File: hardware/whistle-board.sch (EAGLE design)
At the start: 17 parts, among them IC1 MCP4131, IC2 L272, Q1 BC638, Q3 BC638

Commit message: revisions after the most recent draft was assembled and tested
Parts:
- removed Q3: BC638, custom-parts:TRANSISTOR_PNPTO92
- removed R5: 1k, SparkFun-Resistors:1KOHM-1/4W-5%(PTH)
- removed SERIAL: (no value), SparkFun-Connectors:M03PTH
- AUX: device SparkFun-Connectors:M03PTH -> SparkFun-Connectors:M02PTH
- CTL: device SparkFun-Connectors:M02PTH -> SparkFun-Connectors:M04PTH
- Q1: value BC638 -> (none); device custom-parts:TRANSISTOR_PNPTO92 -> custom-parts:TRANSISTOR_NPNTO92
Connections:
- removed net 12V-EN: AUX.3, IC2.V+, Q1.C
- removed net EN: CTL.2, R4.1
- removed net N$5: Q3.B, R5.1
- net 12V: now also IC2.V+; no longer Q1.E
- net 5V: now also D1.C, S1.+; no longer Q3.E
- net CS: now also CTL.2; no longer SERIAL.1
- net DIR: now also R4.2; no longer R5.2
- net GND: now also Q1.E; no longer S1.-
- net N$1: now also Q1.C, S1.-; no longer Q1.B, R4.2
- net N$2: now also Q1.B, R4.1; no longer D1.C, Q3.C, S1.+
- net SCK: now also CTL.3; no longer SERIAL.2
- net SDI: now also CTL.4; no longer SERIAL.3
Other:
- moved on the sheet: D1, D2, IC1, IC2, POW, Q1, R1, R2, R3, R4, S1, TRACK

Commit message: sloppily terminating unused opamp
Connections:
- net GND: now also IC2.IN2+, IC2.IN2-
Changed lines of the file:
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@@
 <label x="58.42" y="66.04" size="1.778" layer="95"/>
+</segment>
+<segment>
+<pinref part="IC2" gate="G$1" pin="IN2+"/>
+<wire x1="25.4" y1="38.1" x2="27.94" y2="38.1" width="0.1524" layer="91"/>
+<label x="30.48" y="38.1" size="1.778" layer="95"/>
+</segment>
+<segment>
+<pinref part="IC2" gate="G$1" pin="IN2-"/>
+<wire x1="25.4" y1="35.56" x2="27.94" y2="35.56" width="0.1524" layer="91"/>
+<label x="30.48" y="35.56" size="1.778" layer="95"/>
 </segment>
 </net>
@@
 </sheet>
 </sheets>
-<errors>
-</errors>
 </schematic>
 </drawing>

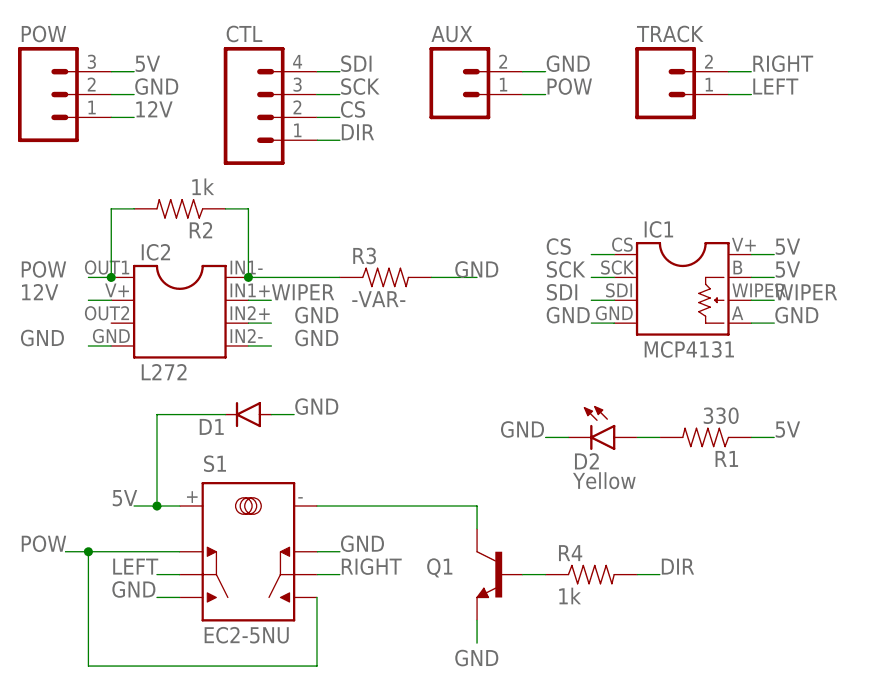
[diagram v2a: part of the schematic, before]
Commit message: adding/fixing diodes, adding silkscreen details
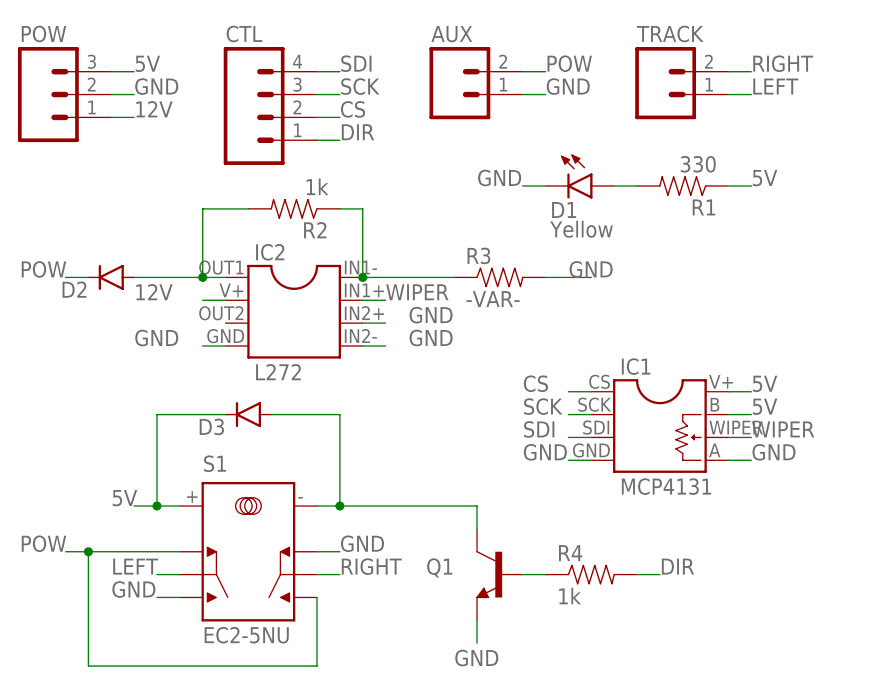
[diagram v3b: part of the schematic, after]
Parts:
- added D3: (no value), SparkFun-DiscreteSemi:DIODE1N4148
- D1: value (none) -> Yellow; device SparkFun-DiscreteSemi:DIODE1N4148 -> custom-parts:LED-YELLOW0603
- D2: value Yellow -> (none); device custom-parts:LED-YELLOW0603 -> SparkFun-DiscreteSemi:DIODEPTH
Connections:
- new net N$5: D2.A, IC2.OUT1, R2.2
- net 5V: now also D3.C; no longer D1.C
- net GND: now also AUX.1, D1.C; no longer AUX.2, D1.A, D2.C
- net N$1: now also D3.A
- net N$19: now also D1.A; no longer D2.A
- net POW: now also AUX.2, D2.C; no longer AUX.1, IC2.OUT1, R2.2
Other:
- moved on the sheet: IC1, IC2, R1, R2, R3

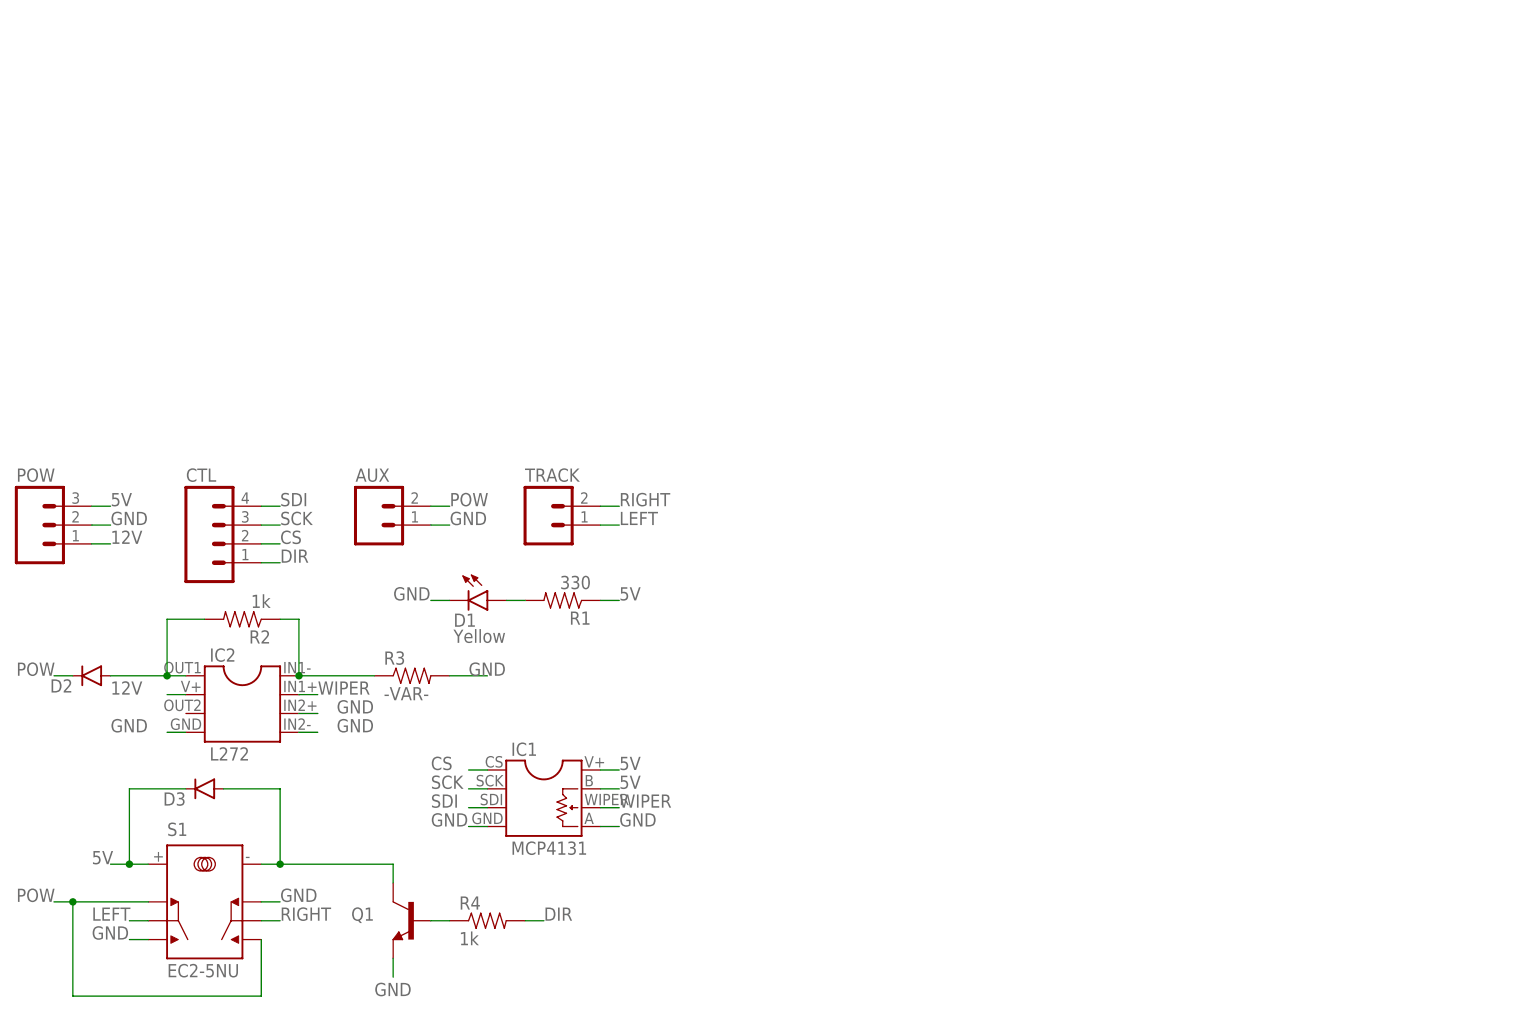
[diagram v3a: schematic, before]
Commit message: Updating license, annotating schematic, updating images, moving software
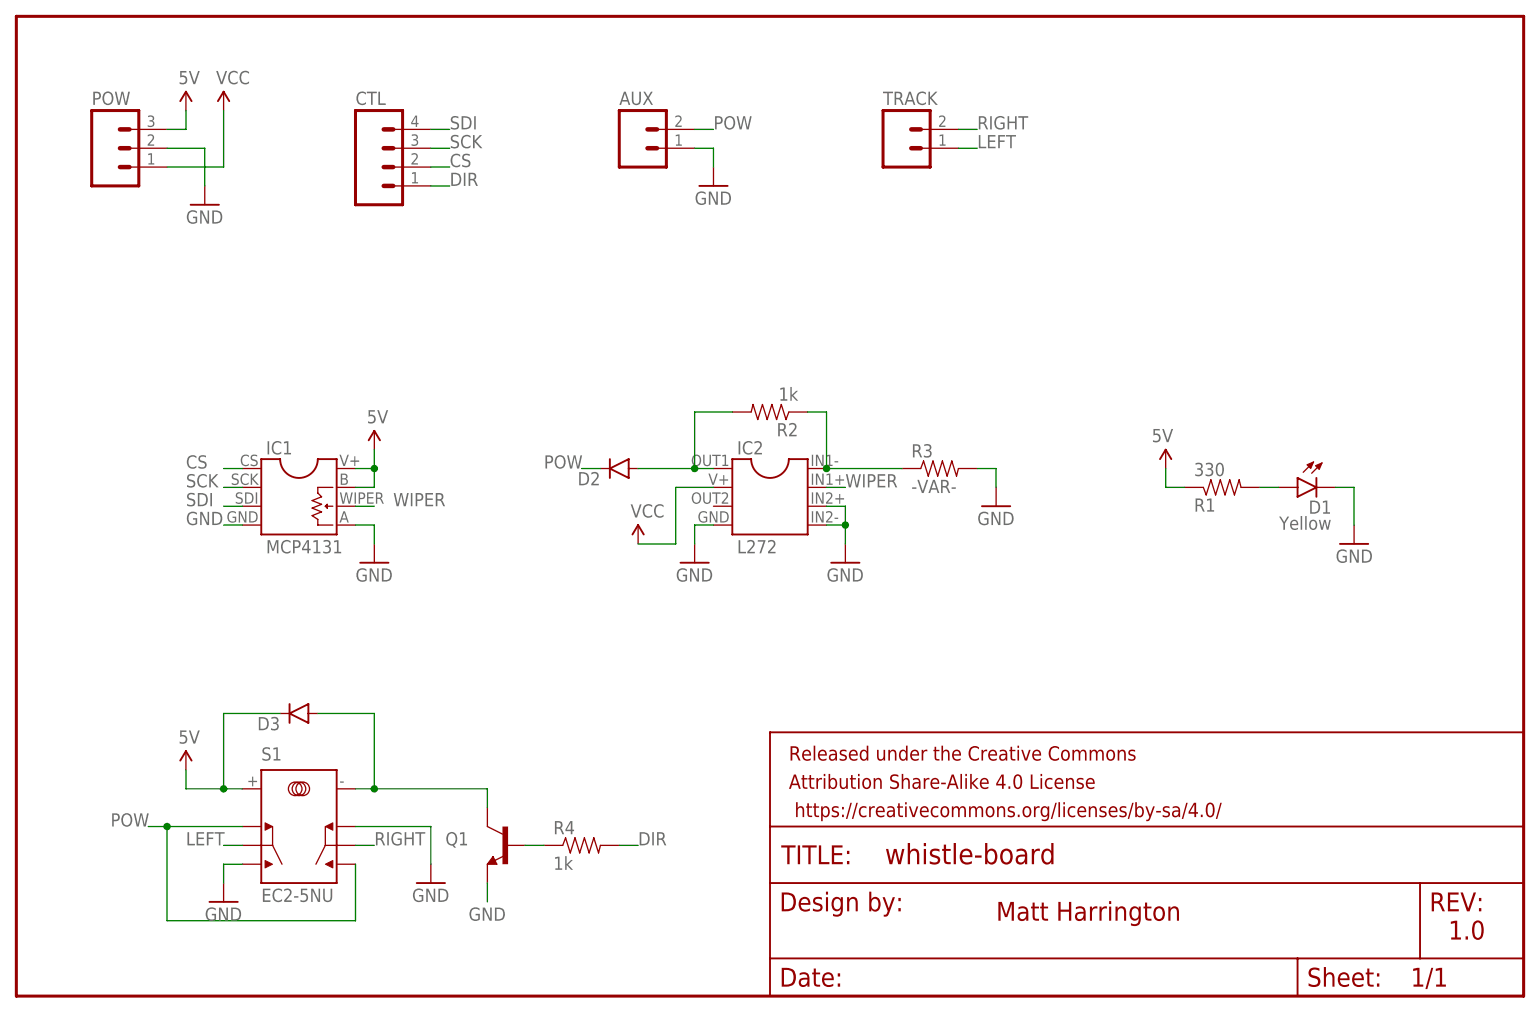
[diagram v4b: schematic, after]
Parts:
- added FRAME1: FRAME-LETTER, SparkFun-Aesthetics:FRAME-LETTER
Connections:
- net 12V renamed VCC
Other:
- note added: "1.0"
- note added: "Matt Harrington"
- moved on the sheet: AUX, CTL, D1, D2, D3, IC1, IC2, POW, Q1, R1, R2, R3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
